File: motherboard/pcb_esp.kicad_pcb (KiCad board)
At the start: 4 copper layers, 77 x 57 mm, 27 parts, among them J1 CONN_01X07, J3 CONN_01X17, J4 CONN_01X13, Q1 S8050, Q2 S8050, U1 LP38691, U2 ESP-12E, U3 USB

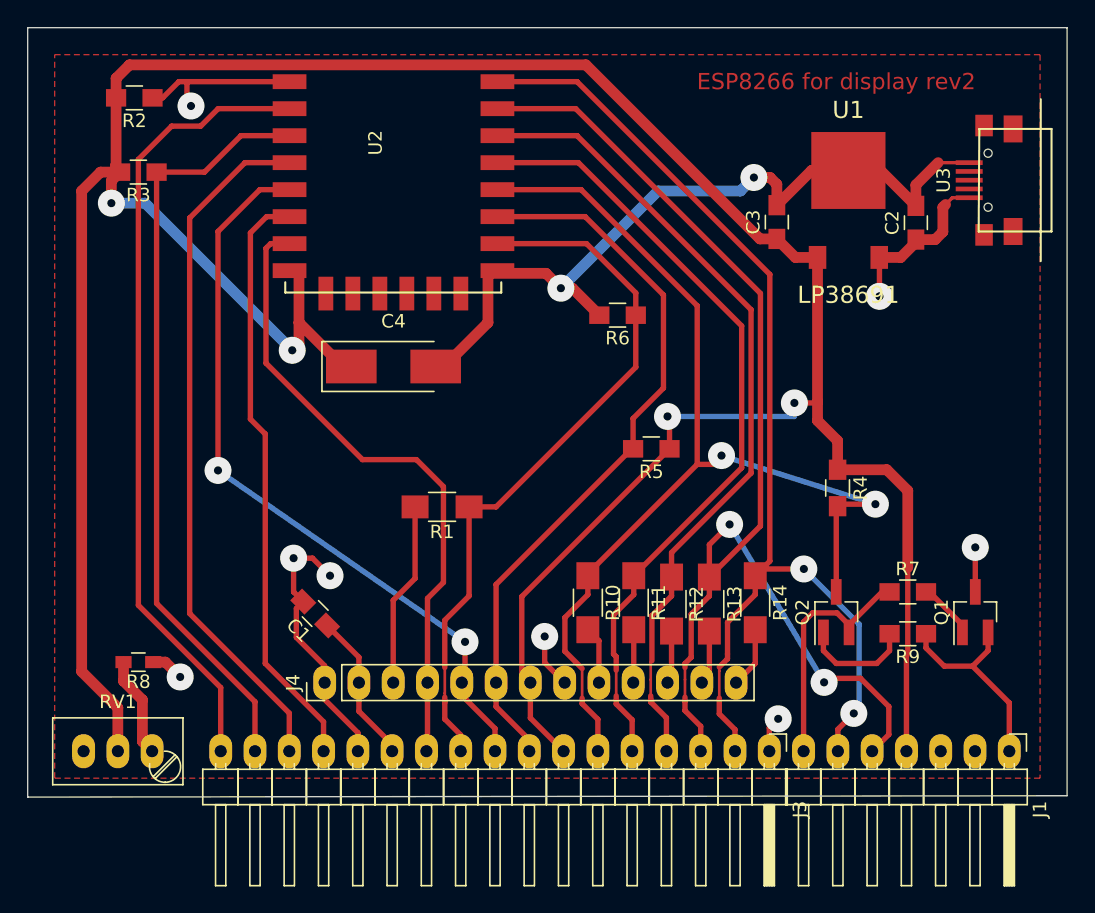
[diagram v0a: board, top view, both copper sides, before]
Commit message: First revision of new, double-sided ESP motherboard for display
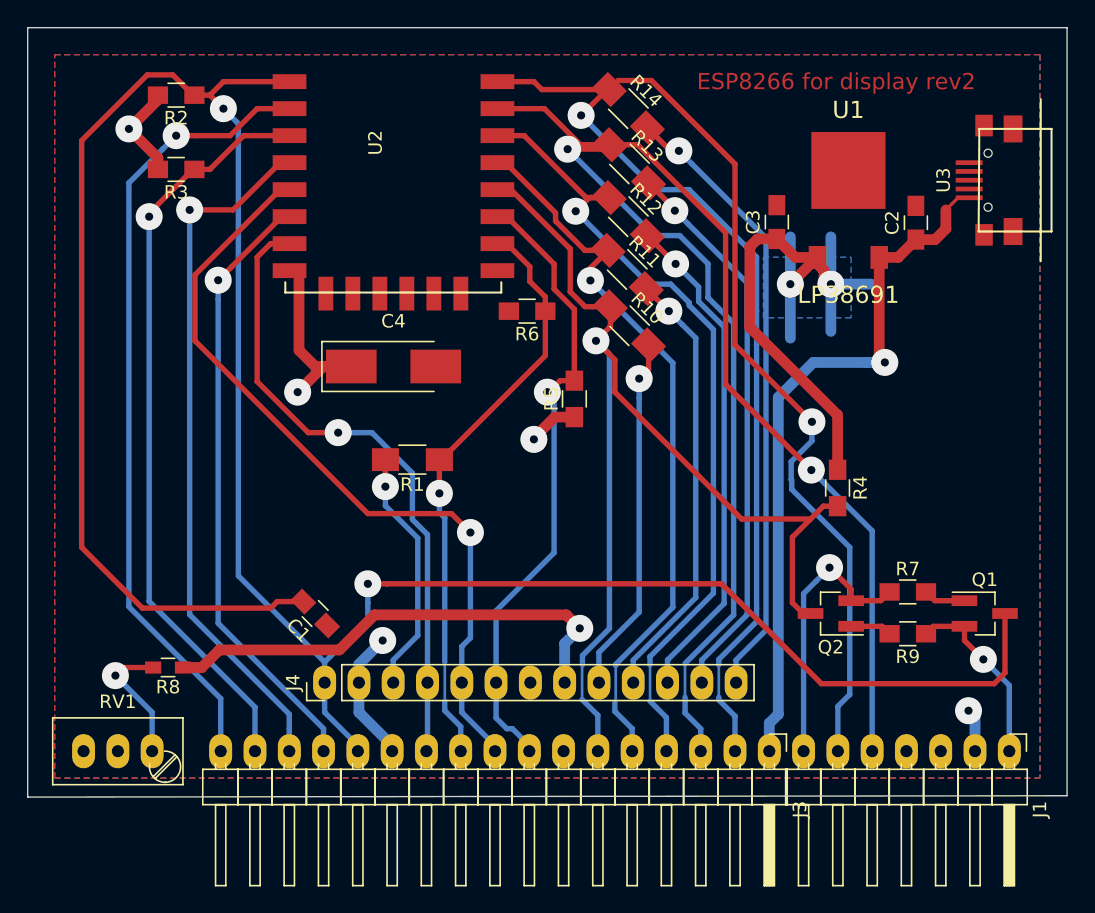
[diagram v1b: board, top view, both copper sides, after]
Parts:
- moved R14 37.8 mm to (92.5, 54.0), turned to 315 degrees
- moved R13 33.1 mm to (92.6, 58.1), turned to 315 degrees
- moved R12 28.9 mm to (92.5, 62.0), turned to 315 degrees
- moved R11 24.7 mm to (92.4, 65.9), turned to 315 degrees
- moved R10 20.7 mm to (92.6, 70.1), turned to 315 degrees
- moved R5 6.80 mm to (88.5, 75.5), turned to 90 degrees
- moved R6 6.71 mm to (85.0, 69.0)
- moved R1 4.13 mm to (76.5, 80.0)
- moved R2 3.11 mm to (59.0, 53.0)
- moved R3 2.81 mm to (59.0, 58.5)
- moved R8 2.24 mm to (58.4, 95.4)
- moved Q1 0.71 mm to (118.9, 91.4), turned to 0 degrees
- moved Q2 0.41 mm to (107.5, 91.4), turned to 180 degrees
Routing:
- net +3V3: track 227.6 -> 73.8 mm, vias 4 -> 5
- net /reset: track 122.7 -> 183.0 mm, vias 4 -> 2
- net GND: track 69.8 -> 13.1 mm
- net /tx_gpio1: track 83.8 -> 128.5 mm
- net /b_down: track 4.51 -> 46.0 mm, vias 0 -> 1
- net /b_select: track 4.05 -> 41.4 mm, vias 0 -> 1
- net /b_right: track 3.94 -> 37.2 mm, vias 0 -> 1
- net /rx_gpio3: track 90.3 -> 120.4 mm
- net /b_up: track 3.94 -> 32.6 mm, vias 0 -> 1
- net /b_left: track 4.26 -> 26.5 mm, vias 0 -> 1
- net /te_gpio15: track 53.9 -> 44.2 mm, vias 0 -> 1
- net /cs_gpio2: track 55.4 -> 47.8 mm, vias 0 -> 1
- net /gpio4: track 59.8 -> 54.4 mm, vias 0 -> 1
- net /rts2: track 8.29 -> 3.08 mm
- net /te: track 13.7 -> 18.3 mm, vias 0 -> 1
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- added copper zone on B.Cu, net +3V3
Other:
- copper layers 4 -> 2

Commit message: Small fixes in routing.
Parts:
- moved C1 32.8 mm to (55.2, 61.8), turned to 90 degrees
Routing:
- net /reset: track 183.0 -> 138.7 mm
- net +3V3: track 73.8 -> 91.6 mm
- net GND: track 13.1 -> 23.0 mm
- net /sda_gpio13: track 48.1 -> 49.1 mm
- net /ch_pd: track 56.6 -> 55.8 mm
- net /adc0: track 59.8 -> 59.1 mm

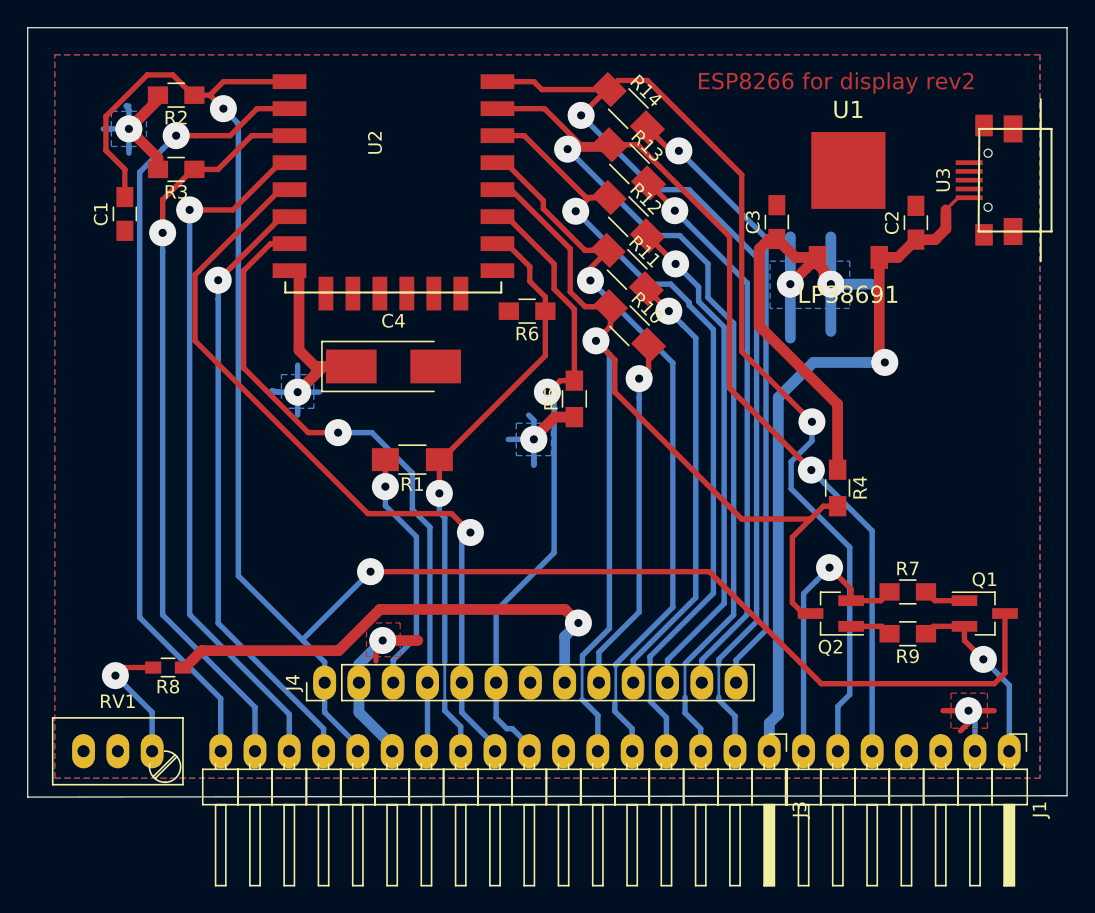
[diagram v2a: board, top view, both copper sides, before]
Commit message: Version rev2 for double-sided etching.
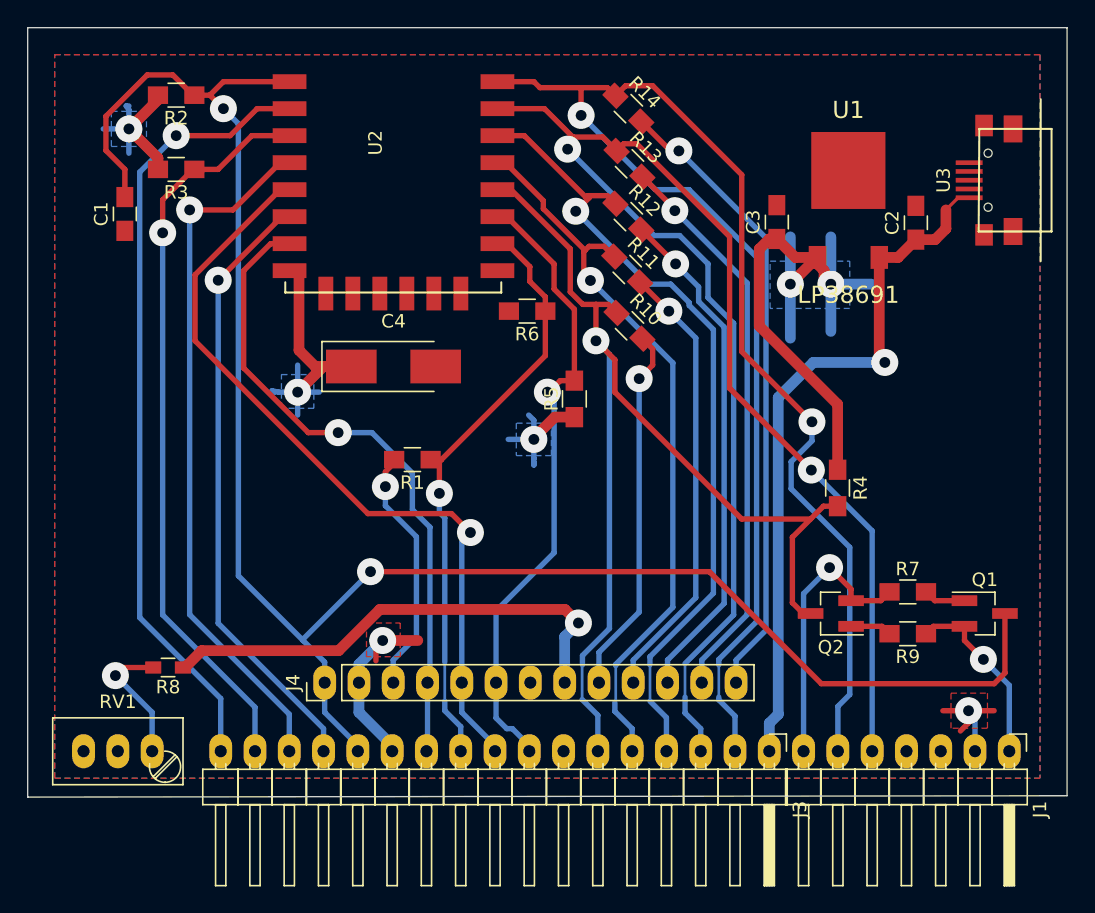
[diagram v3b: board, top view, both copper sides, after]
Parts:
- R1, R10, R11, R12, R13, R14: footprint Resistors_SMD:R_1206_HandSoldering -> Resistors_SMD:R_0805_HandSoldering
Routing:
- net /rx_gpio3: track 120.4 -> 118.6 mm
- net /b_left: track 26.5 -> 27.4 mm
- net /tx_gpio1: track 128.4 -> 127.6 mm
- net /te_gpio15: track 44.2 -> 44.9 mm
- net /b_up: track 32.6 -> 33.3 mm
- net /b_select: track 41.4 -> 42.1 mm
- net /b_down: track 46.0 -> 46.7 mm
- net /b_right: track 37.2 -> 37.8 mm
- net /gpio4: track 54.4 -> 55.0 mm
- net /gpio5: track 61.4 -> 60.9 mm
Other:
- net class Default: via_drill 0.6 -> 0.8

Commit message: Post-rev2 fixes for clearances and zones
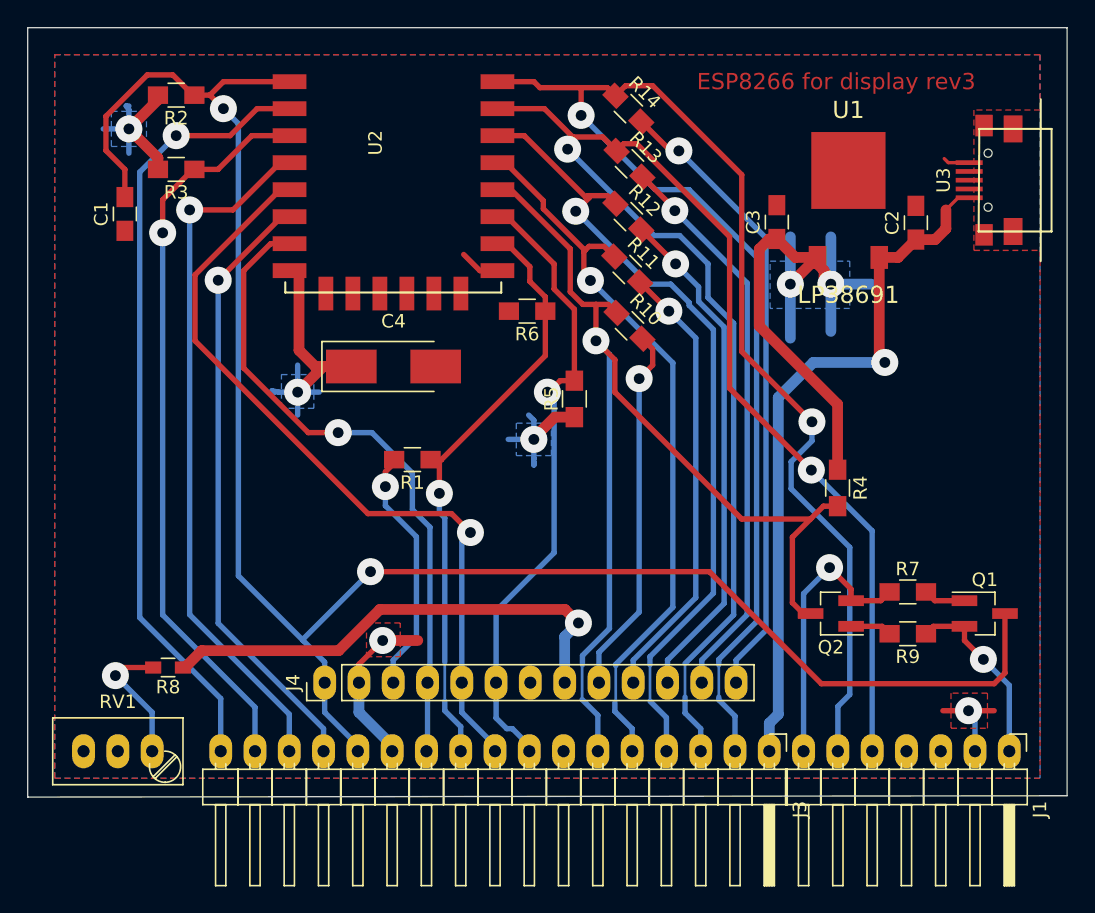
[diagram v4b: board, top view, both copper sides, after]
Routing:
- net GND: track 23.0 -> 23.8 mm
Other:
- board text added: "ESP8266 for display rev3"
- board text removed: "ESP8266 for display rev2"
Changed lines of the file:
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@@
     (user_trace_width 1.5)
     (trace_clearance 0.295)
-    (zone_clearance 0.508)
+    (zone_clearance 0.4)
     (zone_45_only no)
     (trace_min 0.2)
@@
     (visible_elements FFFFFF7F)
     (pcbplotparams
-      (layerselection 0x00000_fffffffe)
+      (layerselection 0x00000_7fffffff)
       (usegerberextensions false)
       (excludeedgelayer true)
@@
       (subtractmaskfromsilk false)
       (outputformat 2)
-      (mirror false)
+      (mirror true)
       (drillshape 1)
       (scaleselection 1)
-      (outputdirectory gerbers5))
+      (outputdirectory gerbers))
   )
   (net 0 "")
@@
     )
   )
-  (gr_text "ESP8266 for display rev2" (at 107.9 52) (layer F.Fab)
+  (gr_text "ESP8266 for display rev3" (at 107.9 52) (layer F.Cu)
     (effects (font (size 1.2 1.2) (thickness 0.25)))
   )
@@
   (gr_line (start 125 48) (end 125 104.9) (layer Edge.Cuts) (width 0.1))
   (gr_line (start 48 48) (end 125 48) (layer Edge.Cuts) (width 0.1))
-  (segment (start 117.7 99.5) (end 117.1 100.1) (width 0.4) (layer F.Cu) (net 1))
-  (segment (start 117.7 98.6) (end 117.7 99.5) (width 0.4) (layer F.Cu) (net 1))
-  (segment (start 73.8 93.9) (end 73.8 94.9) (width 0.4) (layer F.Cu) (net 1))
-  (segment (start 74.3 93.4) (end 73.8 93.9) (width 0.4) (layer F.Cu) (net 1))
-  (segment (start 72.54 96.52) (end 72.54 95.16) (width 0.8) (layer B.Cu) (net 1) (status 10))
-  (segment (start 72.54 95.16) (end 74.3 93.4) (width 0.8) (layer B.Cu) (net 1))
+  (segment (start 72.54 96.52) (end 72.54 95.16) (width 0.4) (layer F.Cu) (net 1))
+  (segment (start 72.54 95.16) (end 74.3 93.4) (width 0.4) (layer F.Cu) (net 1))
+  (segment (start 116.2 58) (end 115.9 57.7) (width 0.25) (layer F.Cu) (net 1))
+  (segment (start 117.75 58) (end 116.2 58) (width 0.25) (layer F.Cu) (net 1))
+  (segment (start 81.5 66) (end 80.3 64.8) (width 0.4) (layer F.Cu) (net 1))
+  (segment (start 82.1 66) (end 81.5 66) (width 0.4) (layer F.Cu) (net 1))
   (segment (start 117.7 98.6) (end 115.8 98.6) (width 0.4) (layer F.Cu) (net 1))
   (segment (start 117.7 98.6) (end 119.6 98.6) (width 0.4) (layer F.Cu) (net 1))
@@
   (via (at 96.241788 57.127523) (size 2) (drill 0.8) (layers F.Cu B.Cu) (net 40))
   (zone (net 1) (net_name GND) (layer F.Cu) (hatch edge 0.508)
-    (connect_pads (clearance 0.3))
-    (min_thickness 0.254)
-    (fill yes (arc_segments 16) (thermal_gap 0.3) (thermal_bridge_width 0.4))
+    (connect_pads (clearance 0.4))
+    (min_thickness 0.5)
+    (fill yes (arc_segments 16) (thermal_gap 0.4) (thermal_bridge_width 0.501))
     (polygon
       (pts
-        (xy 50 50) (xy 123 50) (xy 123 103.6) (xy 50 103.6)
+        (xy 123 54.1) (xy 118.1 54.1) (xy 118.1 64.5) (xy 123 64.5) (xy 123 103.6)
+        (xy 50 103.6) (xy 50 50) (xy 123 50)
       )
     )
     (polygon
       (pts
-        (xy 73.1 92.1) (xy 75.6 92.1) (xy 75.6 94.6) (xy 73.1 94.6)
+        (xy 116.4 97.3) (xy 116.4 99.9) (xy 119.1 99.9) (xy 119.1 97.3)
       )
     )
     (polygon
       (pts
-        (xy 116.4 97.3) (xy 119.1 97.3) (xy 119.1 99.9) (xy 116.4 99.9)
+        (xy 73.1 92.1) (xy 73.1 94.6) (xy 75.6 94.6) (xy 75.6 92.1)
       )
     )
   )
   (zone (net 2) (net_name +3V3) (layer B.Cu) (hatch edge 0.508)
-    (connect_pads (clearance 0.3))
-    (min_thickness 0.254)
-    (fill yes (arc_segments 16) (thermal_gap 0.3) (thermal_bridge_width 0.4))
+    (connect_pads (clearance 0.4))
+    (min_thickness 0.5)
+    (fill yes (arc_segments 16) (thermal_gap 0.4) (thermal_bridge_width 0.501))
     (polygon
       (pts
